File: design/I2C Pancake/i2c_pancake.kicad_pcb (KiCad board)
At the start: 4 copper layers, 74.9 x 45 mm, 44 parts, among them J1 Conn_01x03, J2 Conn_01x03, J3 Conn_01x05_Male, J4 Conn_01x04, J5 Conn_01x04, J6 Conn_01x04, J7 Conn_01x05_Male, J8 Conn_01x05_Female, SW1 SW_DIP_x04, U1 INA826, U2 TL750M10CKVU, U3 INA826, U4 INA826, U6 PIC16F1826-ISO

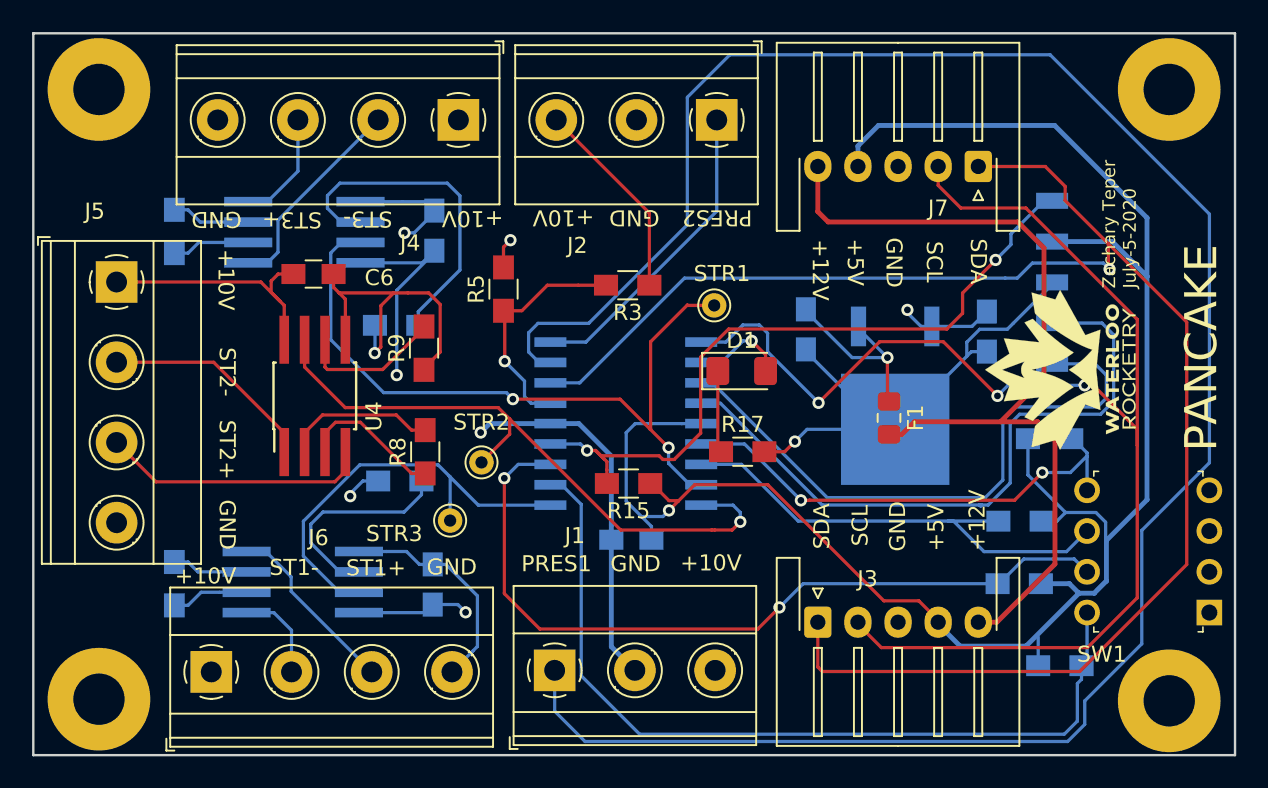
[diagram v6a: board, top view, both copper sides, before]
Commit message: Implement improvements suggested by Zachariah Mears and update Gerbers
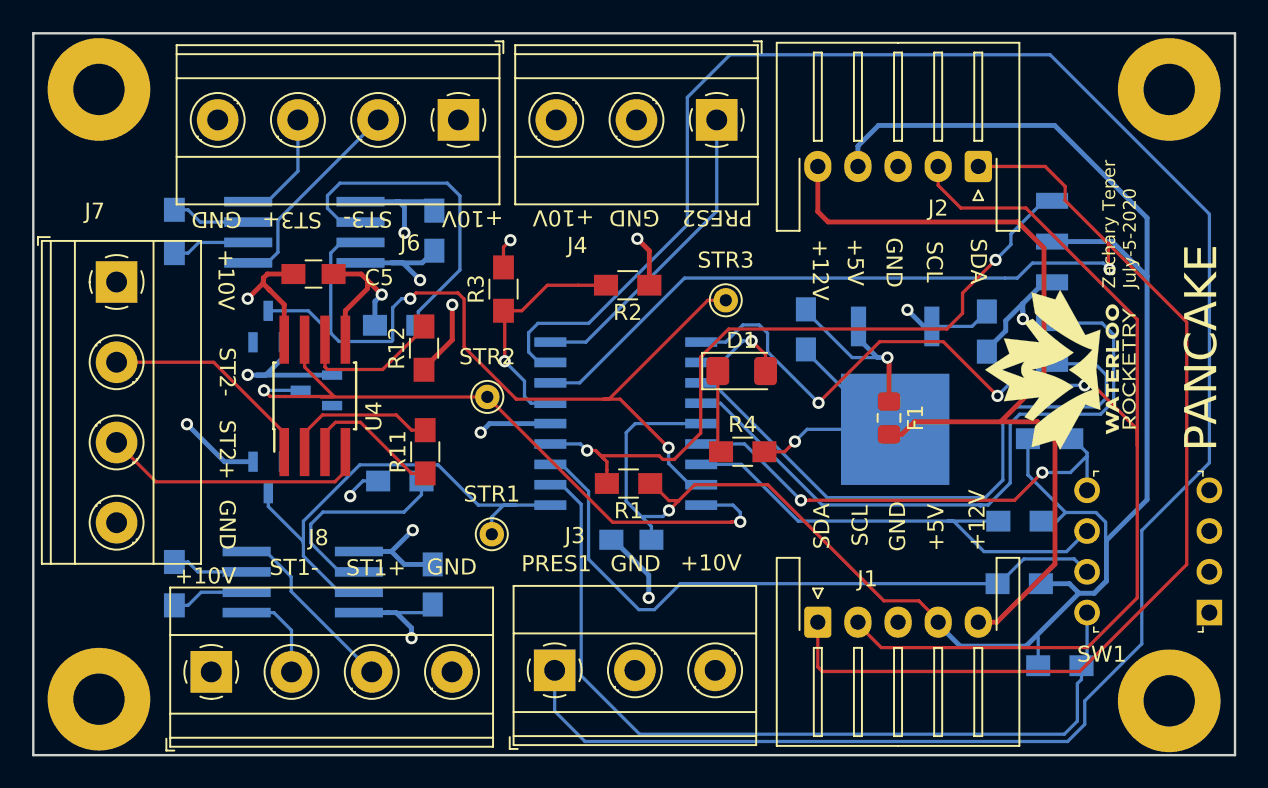
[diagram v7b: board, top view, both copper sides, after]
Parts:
- added D2: PLVA650A,215, footprints:SOT95P230X110-3N, B.Cu at (104.3, 107.5)
- added D3: PLVA650A,215, footprints:SOT95P230X110-3N, B.Cu at (107.3, 111.5)
- added D4: PLVA650A,215, footprints:SOT95P230X110-3N, B.Cu at (104.3, 116.9)
- R2: renamed from R3; value 5K -> 10K
- R3: renamed from R5; value 10K -> 5K
- U1: renamed from U2; value TL750M10CKVU -> KVU3
- moved STR3 26.2 mm to (132.8, 102.9), turned to 0 degrees
- moved STR1 19.9 mm to (118.2, 117.5)
- moved STR2 4.09 mm to (118.0, 108.9)
- renumbered C3 to C2, C8 to C3, C5 to C4, C6 to C5, C2 to C6, J3 to J1, J7 to J2, J1 to J3, J2 to J4, J8 to J5, J4 to J6, J5 to J7, J6 to J8, R15 to R1, R7 to R10, R8 to R11, R9 to R12, R2 to R13, R4 to R14, R17 to R4, R12 to R5, R13 to R6, R14 to R7, R16 to R8, R6 to R9, U6 to U2, U1 to U5
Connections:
- STR1 pad 1: /STRAIN_OUT_1 -> /STRAIN_OUT_3
- STR3 pad 1: /STRAIN_OUT_3 -> /STRAIN_OUT_1
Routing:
- net +10V: track 55.5 -> 31.9 mm, vias 3 -> 5
- net GND: track 103.9 -> 83.1 mm, vias 6 -> 12
- net /STRAIN_OUT_1: track 45.3 -> 54.8 mm
- net /DIP_2: track 49.8 -> 41.3 mm, vias 2 -> 0
- net /STRAIN_OUT_3: track 27.2 -> 31.4 mm
- net /STRAIN_OUT_2: track 40.2 -> 44.0 mm, vias 1 -> 2
- net Net-(C1-Pad1): track 11.4 -> 12.4 mm

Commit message: Replace linear regulator to match the recent Digikey order
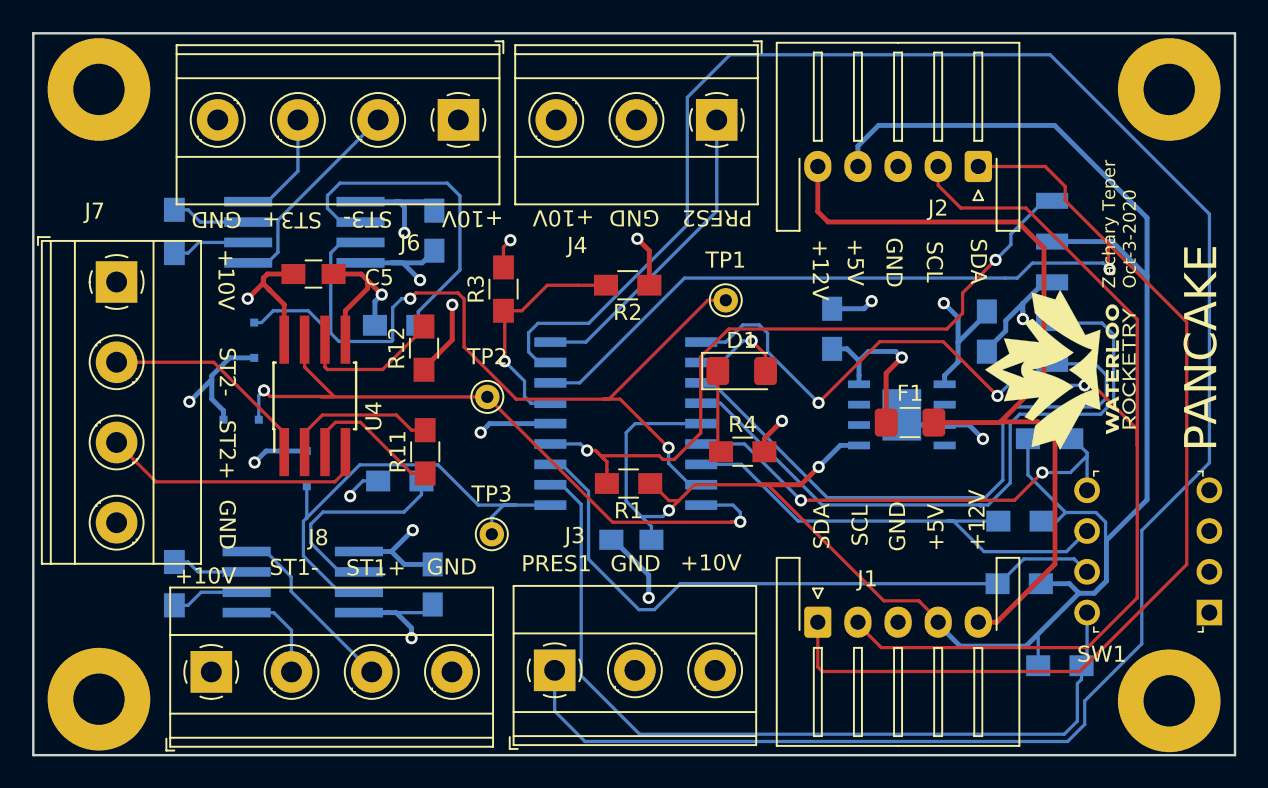
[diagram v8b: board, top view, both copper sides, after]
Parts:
- C1: value 0.1 uF -> 10 uF
- D2, D3, D4: value PLVA650A,215 -> DDZ4V7ASF-7; footprint footprints:SOT95P230X110-3N -> Diode_SMD:D_SOD-323F
- F1: footprint Fuse:Fuse_0805_2012Metric_Pad1.15x1.40mm_HandSolder -> Fuse:Fuse_1206_3216Metric_Pad1.42x1.75mm_HandSolder
- U1: value KVU3 -> BDJ0FC0WEFJ-E2; footprint footprints:TL750M10CKVU -> footprints:BDJ0FC0WEFJ-E2
- moved D3 5.03 mm to (102.6, 113.3), turned to 180 degrees
- moved D4 2.46 mm to (106.7, 116.4), turned to 90 degrees
- moved C1 1.63 mm to (139.4, 107.7), turned to 90 degrees
- moved F1 1.34 mm to (144.3, 113.5), turned to 0 degrees
- moved D2 1.22 mm to (103.4, 108.4), turned to 270 degrees
- moved U1 0.99 mm to (143.8, 113.0), turned to 180 degrees
- renumbered STR3 to TP1, STR2 to TP2, STR1 to TP3
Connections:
- D2 pad 1: GND -> /STRAIN_OUT_1
- D2 pad 2: (no net) -> GND
- D3 pad 1: GND -> /STRAIN_OUT_2
- D3 pad 2: (no net) -> GND
- D4 pad 1: GND -> /STRAIN_OUT_3
- D4 pad 2: (no net) -> GND
- U1 pad 1: Net-(C1-Pad1) -> +10V
- U1 pad 2: GND -> Net-(U1-Pad2)
- U1 pad 3: +10V -> GND
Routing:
- net GND: track 83.1 -> 75.7 mm, vias 12 -> 14
- net +5V: track 123.6 -> 130.7 mm, vias 1 -> 2
- net +12V: track 55.6 -> 52.5 mm
- net +10V: track 31.9 -> 34.2 mm
- net /STRAIN_OUT_3: track 31.4 -> 29.3 mm
- net Net-(C1-Pad1): track 12.4 -> 11.0 mm
- net /STRAIN_OUT_1: track 54.8 -> 56.0 mm
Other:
- board text added: "Zachary Teper Oct-3-2020"
- board text removed: "Zachary Teper July-5-2020"
